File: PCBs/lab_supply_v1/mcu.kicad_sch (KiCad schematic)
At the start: 0 parts

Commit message: Updated PCB, FTDI interface
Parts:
- added C37, C38, C48: 2.2uF, symbol Device:C
- added C39, C40, C41, C42, C45, C46, C47, C49: 100nF, symbol Device:C
- added C43, C44: 1.2pF, symbol Device:C
- added D10, D9: RED, symbol Device:LED
- added FB1: Ferrite_Bead, symbol PCM_Device_AKL:Ferrite_Bead
- added L4: 1.8nH, symbol Device:L
- added R26, R27, R28: 1kR, symbol Device:R_Small
- added R29: 0R, symbol Device:R_Small
- added SW1: EN, symbol Switch:SW_Push
- added U13: ESP32-PICO-D4, Package_DFN_QFN:QFN-48-1EP_7x7mm_P0.5mm_EP5.3x5.3mm, symbol MCU_Espressif:ESP32-PICO-D4
- added U15: FT232RL, Package_SO:SSOP-28_5.3x10.2mm_P0.65mm, symbol Interface_USB:FT232RL
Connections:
- new net: R29.1, U13.26 (VDD_SDIO)
- new net: C38.1, C39.1, C40.1, C41.1, C42.1, FB1.2, U13.1 (VDDA), U13.19 (VDD3P3_RTC), U13.3 (VDDA3P3), U13.37 (VDD3P3_CPU), U13.4 (VDDA3P3), U13.43 (VDDA), U13.46 (VDDA)
- new net: C48.1, R28.2, SW1.2, U13.9 (EN)
- new net: D10.2 (A), R26.1
- new net: D9.2 (A), R27.1
- new net: C43.1, L4.1, U13.2 (LNA_IN)
- new net: C47.1, U15.17 (3V3OUT)
- new net +3.3V: C37.1, C45.1, C46.1, C49.1, FB1.1, R26.2, R27.2, R28.1, R29.2, U15.20 (VCC), U15.4 (VCCIO)
- new net Antenna: C44.1, L4.2
- new net D+: U15.15 (USBD+)
- new net D-: U15.16 (USBD-)
- new net GND: C37.2, C38.2, C39.2, C40.2, C41.2, C42.2, C43.2, C44.2, C45.2, C46.2, C47.2, C48.2, C49.2, SW1.1, U13.49 (GND), U15.18 (GND), U15.21 (GND), U15.25 (AGND), U15.7 (GND)
- new net MCU_CTS: U13.21 (IO15), U15.11 (CTS)
- new net MCU_RTS: U13.20 (IO13), U15.3 (RTS)
- new net MCU_RX: U13.40 (U0RXD/IO3), U15.1 (TXD)
- new net MCU_TX: U13.41 (U0TXD/IO1), U15.5 (RXD)
- new net RX_LED: D10.1 (K), U15.22 (CBUS1)
- new net TX_LED: D9.1 (K), U15.23 (CBUS0)
- no-connect marks 0 -> 13

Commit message: Updated PCB added current sense buffer added ADC/DAC for current/voltage sensing added ACDC converter bypass made optimal supply voltage 36 V @ 5 A
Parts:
- added J6: FAN_OUT, symbol Connector:Screw_Terminal_01x02
- added U16: MCP4922-ESL, PCM_Package_SO_AKL:SOIC-14_3.9x8.7mm_P1.27mm, symbol Analog_DAC:MCP4922-ESL
- added U17: MCP3202, symbol Analog_ADC:MCP3202
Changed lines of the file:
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@@
+	)
+	(symbol
+		(lib_id "Connector:Screw_Terminal_01x02")
+		(at 228.6 133.35 0)
+		(unit 1)
+		(exclude_from_sim no)
+		(in_bom yes)
+		(on_board yes)
+		(dnp no)
+		(fields_autoplaced yes)
+		(property "Reference" "J6"
+			(at 231.14 133.3499 0)
+			(effects
+				(font
+					(size 1.27 1.27)
+				)
+				(justify left)
+			)
+		)
+		(property "Value" "FAN_OUT"
+			(at 231.14 135.8899 0)
+			(effects
+				(font
+					(size 1.27 1.27)
+				)
+				(justify left)
+			)
+		)
+		(property "Footprint" ""
+			(at 228.6 133.35 0)
+			(effects
+				(font
+					(size 1.27 1.27)
+				)
+				(hide yes)
+			)
+		)
+		(property "Datasheet" "~"
+			(at 228.6 133.35 0)
+			(effects
+				(font
+					(size 1.27 1.27)
+				)
+				(hide yes)
+			)
+		)
+		(property "Description" "Generic screw terminal, single row, 01x02, script generated (kicad-library-utils/schlib/autogen/connector/)"
+			(at 228.6 133.35 0)
+			(effects
+				(font
+					(size 1.27 1.27)
+				)
+				(hide yes)
+			)
+		)
+		(pin "2"
+		)
+		(pin "1"
+		)
+		(instances
+			(project "lab_supply_v1"
+				(path "/c381ddef-a21e-4847-9921-7e6cff5e49a3/01eef697-a715-4e9d-9e7c-e0556cbb5130"
+					(reference "J6")
+					(unit 1)
+				)
+			)
+		)
 	)
 	(symbol
@@
 	)
 	(symbol
+		(lib_id "Analog_ADC:MCP3202")
+		(at 66.04 143.51 180)
+		(unit 1)
+		(exclude_from_sim no)
+		(in_bom yes)
+		(on_board yes)
+		(dnp no)
+		(fields_autoplaced yes)
+		(property "Reference" "U17"
+			(at 69.0565 128.27 0)
+			(effects
+				(font
+					(size 1.27 1.27)
+				)
+				(justify right)
+			)
+		)
+		(property "Value" "MCP3202"
+			(at 69.0565 130.81 0)
+			(effects
+				(font
+					(size 1.27 1.27)
+				)
+				(justify right)
+			)
+		)
+		(property "Footprint" ""
+			(at 66.04 140.97 0)
+			(effects
+				(font
+					(size 1.27 1.27)
+				)
+				(hide yes)
+			)
+		)
+		(property "Datasheet" "http://ww1.microchip.com/downloads/en/DeviceDoc/21034D.pdf"
+			(at 66.04 148.59 0)
+			(effects
+				(font
+					(size 1.27 1.27)
+				)
+				(hide yes)
+			)
+		)
+		(property "Description" "A/D Converter, 12-Bit, 2-Channel, SPI Interface, 2.7V-5.5V"
+			(at 66.04 143.51 0)
+			(effects
+				(font
+					(size 1.27 1.27)
+				)
+				(hide yes)
+			)
+		)
+		(pin "2"
+		)
+		(pin "4"
+		)
+		(pin "5"
+		)
+		(pin "6"
+		)
+		(pin "1"
+		)
+		(pin "3"
+		)
+		(pin "7"
+		)
+		(pin "8"
+		)
+		(instances
+			(project "lab_supply_v1"
+				(path "/c381ddef-a21e-4847-9921-7e6cff5e49a3/01eef697-a715-4e9d-9e7c-e0556cbb5130"
+					(reference "U17")
+					(unit 1)
+				)
+			)
+		)
+	)
+	(symbol
 		(lib_id "power:GND")
 		(at 62.23 35.56 0)
@@
 					(unit 1)
 				)
+			)
+		)
+	)
+	(symbol
+		(lib_id "Analog_DAC:MCP4922-ESL")
+		(at 62.23 175.26 0)
+		(unit 1)
+		(exclude_from_sim no)
+		(in_bom yes)
+		(on_board yes)
+		(dnp no)
+		(fields_autoplaced yes)
+		(property "Reference" "U16"
+			(at 86.36 163.8614 0)
+			(effects
+				(font
+					(size 1.27 1.27)
+				)
+			)
+		)
+		(property "Value" "MCP4922-ESL"
+			(at 86.36 166.4014 0)
+			(effects
+				(font
+					(size 1.27 1.27)
+				)
+			)
+		)
+		(property "Footprint" "PCM_Package_SO_AKL:SOIC-14_3.9x8.7mm_P1.27mm"
+			(at 62.23 175.26 0)
+			(effects
+				(font
+					(size 1.27 1.27)
+					(italic yes)
+				)
+				(hide yes)
+			)
+		)
+		(property "Datasheet" "http://ww1.microchip.com/downloads/en/devicedoc/21897a.pdf"
+			(at 62.23 175.26 0)
+			(effects
+				(font
+					(size 1.27 1.27)
+				)
+				(hide yes)
+			)
+		)
+		(property "Description" "Dual 12-bit Digital to Analog Converter, SPI Interface, SOIC-14"
+			(at 62.23 175.26 0)
+			(effects
+				(font
+					(size 1.27 1.27)
+				)
+				(hide yes)
+			)
+		)
+		(pin "3"
+		)
+		(pin "4"
+		)
+		(pin "1"
+		)
+		(pin "10"
+		)
+		(pin "12"
+		)
+		(pin "5"
+		)
+		(pin "2"
+		)
+		(pin "6"
+		)
+		(pin "7"
+		)
+		(pin "8"
+		)
+		(pin "9"
+		)
+		(pin "11"
+		)
+		(pin "13"
+		)
+		(pin "14"
+		)
+		(instances
+			(project "lab_supply_v1"
+				(path "/c381ddef-a21e-4847-9921-7e6cff5e49a3/01eef697-a715-4e9d-9e7c-e0556cbb5130"
+					(reference "U16")
+					(unit 1)
+				)

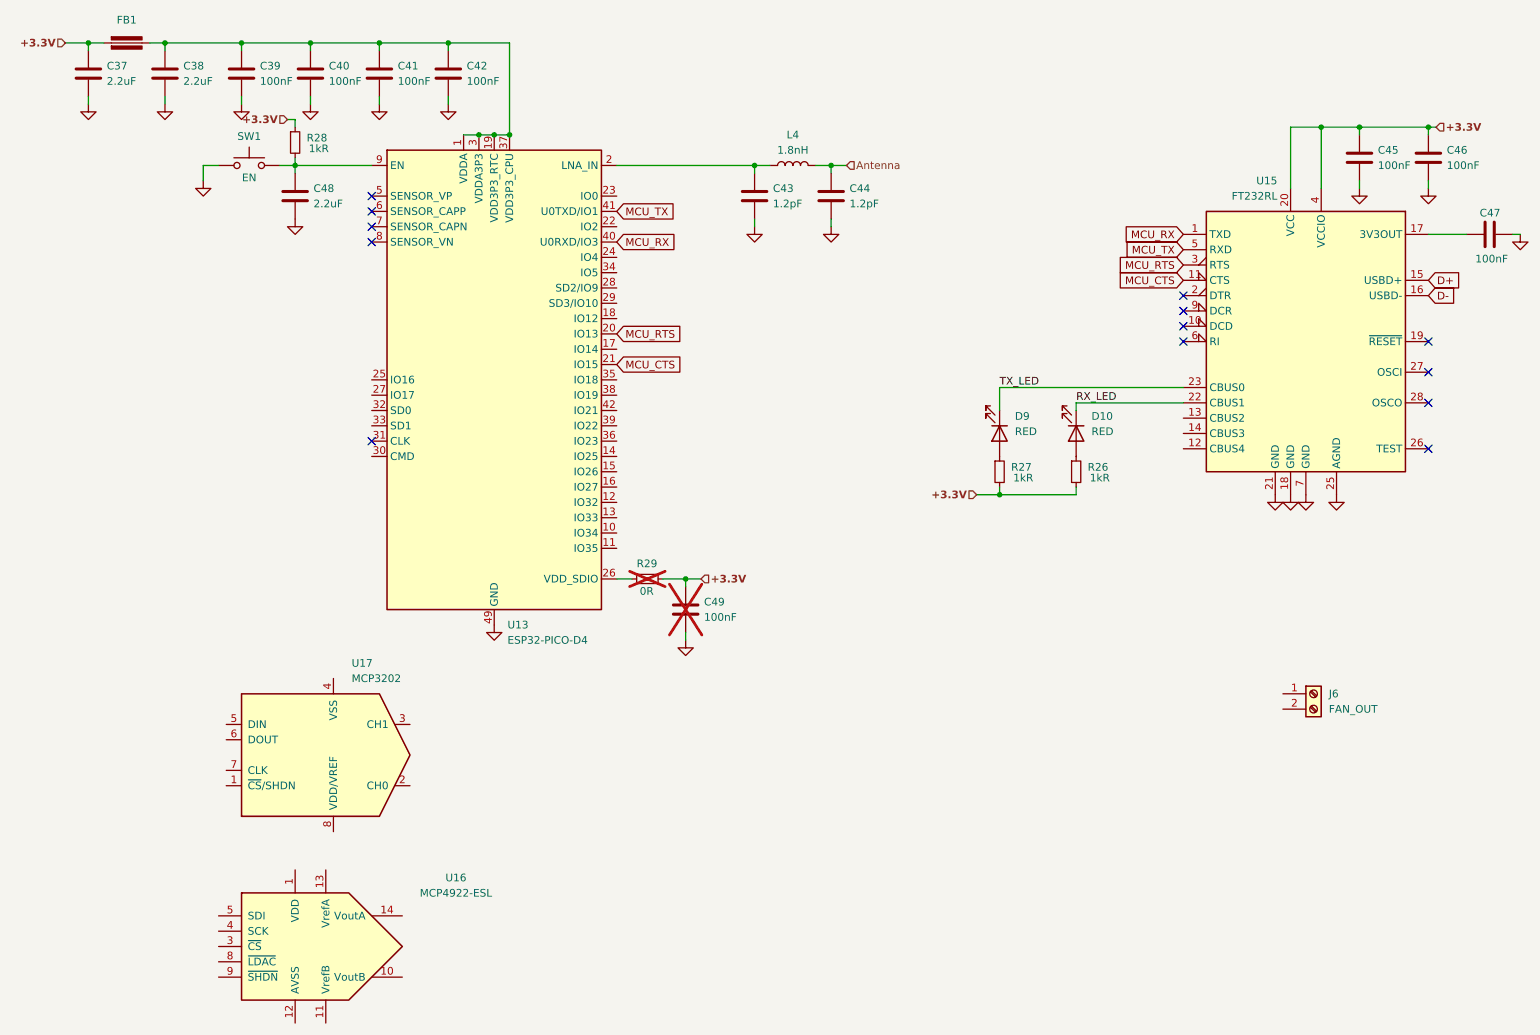
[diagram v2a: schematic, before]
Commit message: Changed MCU to ESP32 WROOM module Added constant current source (3.3 A max, 150 W)
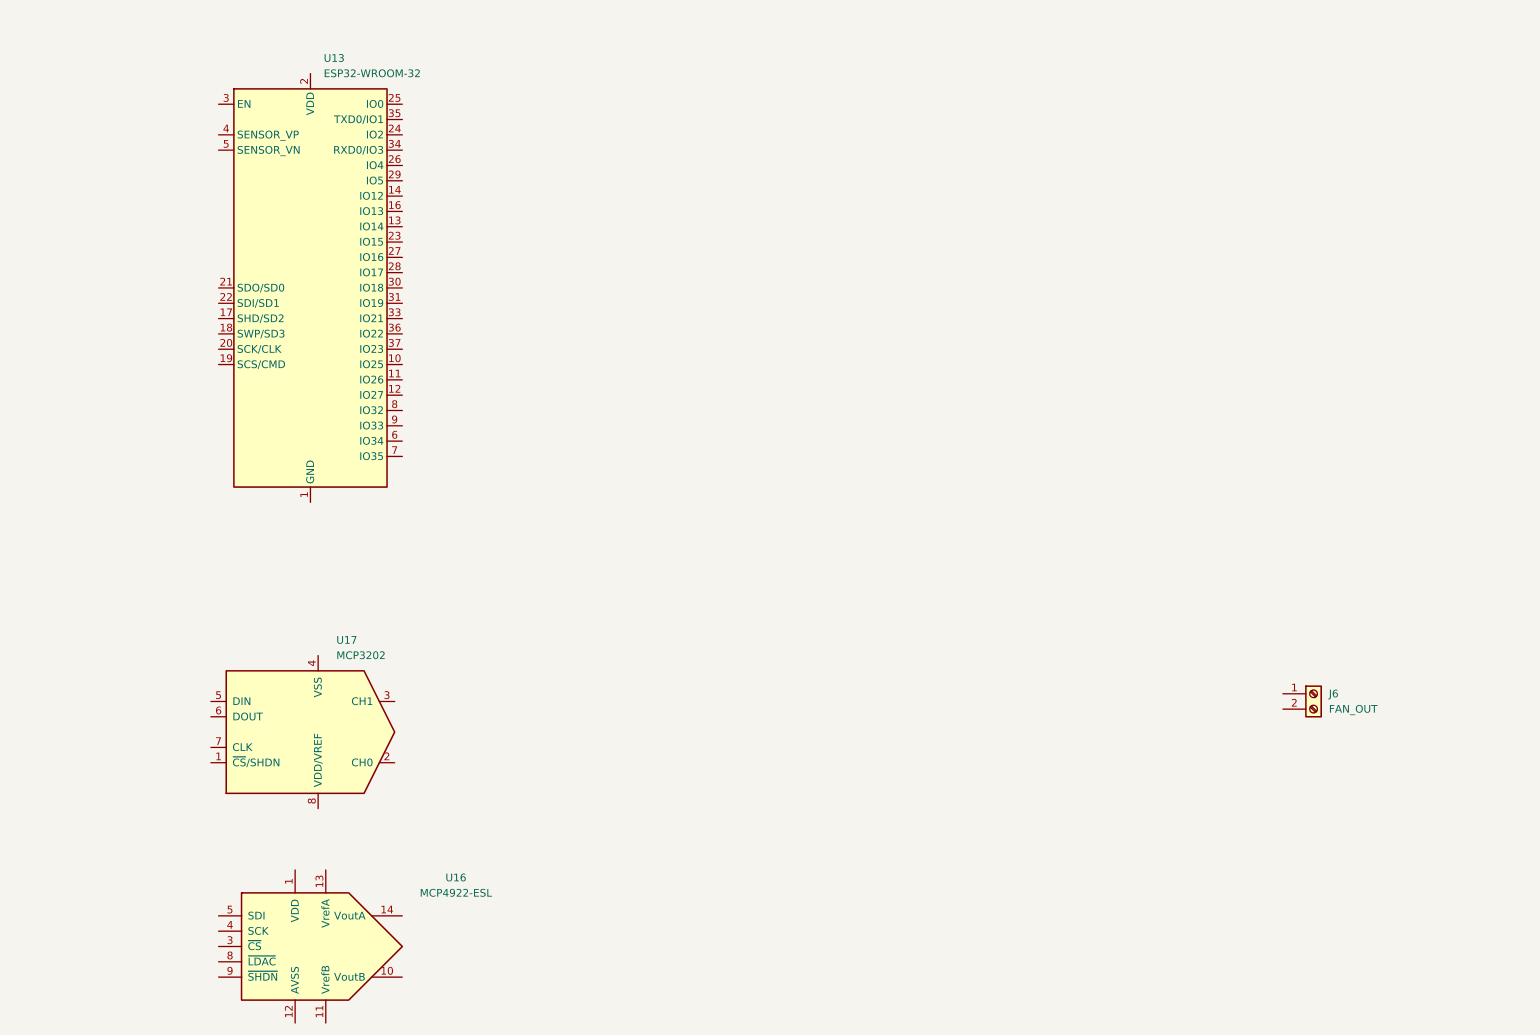
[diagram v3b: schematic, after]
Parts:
- removed C37, C38, C48: 2.2uF, symbol Device:C
- removed C39, C40, C41, C42, C45, C46, C47, C49: 100nF, symbol Device:C
- removed C43, C44: 1.2pF, symbol Device:C
- removed D10, D9: RED, symbol Device:LED
- removed FB1: Ferrite_Bead, symbol PCM_Device_AKL:Ferrite_Bead
- removed L4: 1.8nH, symbol Device:L
- removed R26, R27, R28: 1kR, symbol Device:R_Small
- removed R29: 0R, symbol Device:R_Small
- removed SW1: EN, symbol Switch:SW_Push
- removed U13: ESP32-PICO-D4, Package_DFN_QFN:QFN-48-1EP_7x7mm_P0.5mm_EP5.3x5.3mm, symbol MCU_Espressif:ESP32-PICO-D4
- removed U15: FT232RL, Package_SO:SSOP-28_5.3x10.2mm_P0.65mm, symbol Interface_USB:FT232RL
- added U13: ESP32-WROOM-32, RF_Module:ESP32-WROOM-32, symbol RF_Module:ESP32-WROOM-32
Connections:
- new net: U13.1 (GND), U13.15 (GND), U13.38 (GND), U13.39 (GND)
- no-connect marks 13 -> 0
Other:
- moved on the sheet: U17

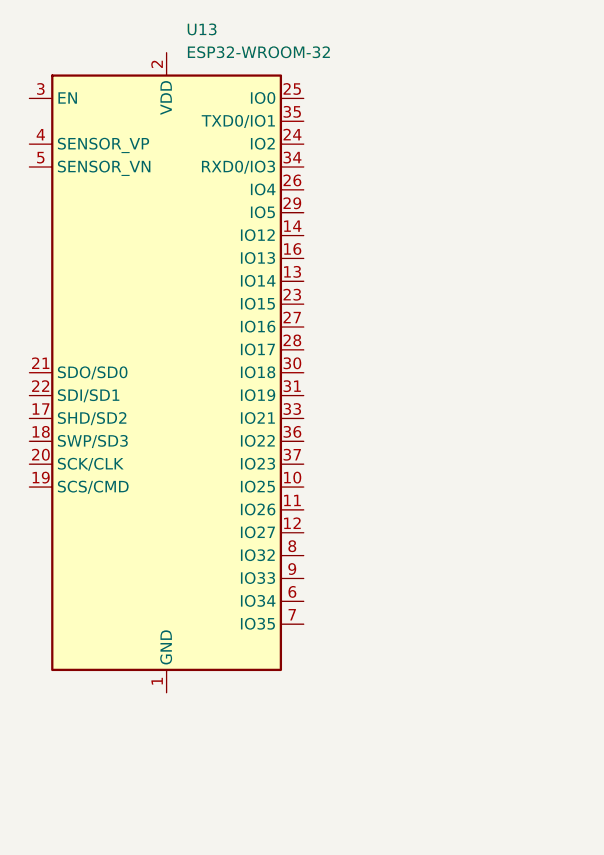
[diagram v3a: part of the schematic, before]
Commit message: added more info to CC sink updated ESP module to fit HiLetgo's ESP32-WROOM
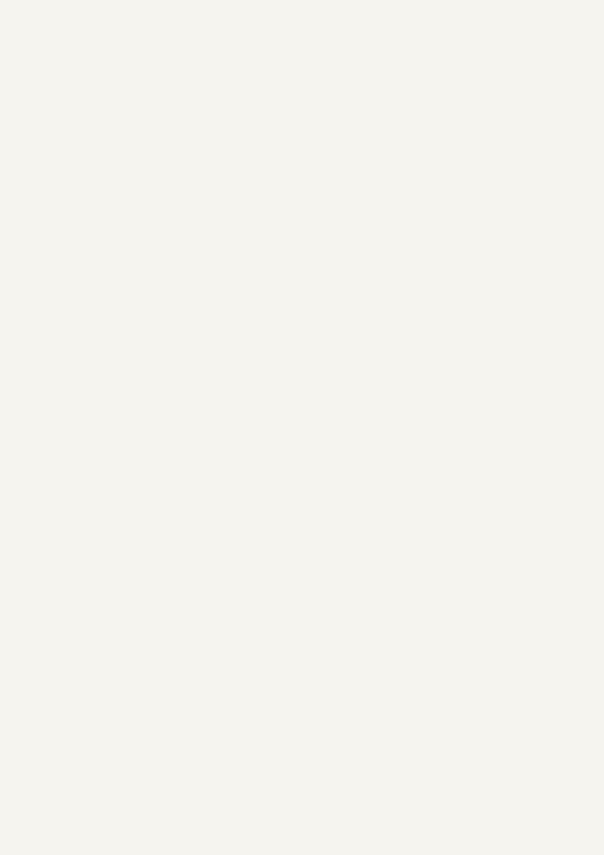
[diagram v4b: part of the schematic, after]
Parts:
- removed U13: ESP32-WROOM-32, RF_Module:ESP32-WROOM-32, symbol RF_Module:ESP32-WROOM-32
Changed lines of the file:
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@@
 	(paper "A4")
-	(symbol
-		(lib_id "RF_Module:ESP32-WROOM-32")
-		(at 62.23 66.04 0)
-		(unit 1)
-		(exclude_from_sim no)
-		(in_bom yes)
-		(on_board yes)
-		(dnp no)
-		(fields_autoplaced yes)
-		(property "Reference" "U13"
-			(at 64.4241 27.94 0)
-			(effects
-				(font
-					(size 1.27 1.27)
-				)
-				(justify left)
-			)
-		)
-		(property "Value" "ESP32-WROOM-32"
-			(at 64.4241 30.48 0)
-			(effects
-				(font
-					(size 1.27 1.27)
-				)
-				(justify left)
-			)
-		)
-		(property "Footprint" "RF_Module:ESP32-WROOM-32"
-			(at 62.23 104.14 0)
-			(effects
-				(font
-					(size 1.27 1.27)
-				)
-				(hide yes)
-			)
-		)
-		(property "Datasheet" "https://www.espressif.com/sites/default/files/documentation/esp32-wroom-32_datasheet_en.pdf"
-			(at 54.61 64.77 0)
-			(effects
-				(font
-					(size 1.27 1.27)
-				)
-				(hide yes)
-			)
-		)
-		(property "Description" "RF Module, ESP32-D0WDQ6 SoC, Wi-Fi 802.11b/g/n, Bluetooth, BLE, 32-bit, 2.7-3.6V, onboard antenna, SMD"
-			(at 62.23 66.04 0)
-			(effects
-				(font
-					(size 1.27 1.27)
-				)
-				(hide yes)
-			)
-		)
-		(pin "11"
-		)
-		(pin "16"
-		)
-		(pin "10"
-		)
-		(pin "37"
-		)
-		(pin "35"
-		)
-		(pin "15"
-		)
-		(pin "32"
-		)
-		(pin "28"
-		)
-		(pin "24"
-		)
-		(pin "12"
-		)
-		(pin "22"
-		)
-		(pin "36"
-		)
-		(pin "18"
-		)
-		(pin "2"
-		)
-		(pin "27"
-		)
-		(pin "20"
-		)
-		(pin "31"
-		)
-		(pin "9"
-		)
-		(pin "7"
-		)
-		(pin "39"
-		)
-		(pin "17"
-		)
-		(pin "29"
-		)
-		(pin "26"
-		)
-		(pin "8"
-		)
-		(pin "19"
-		)
-		(pin "14"
-		)
-		(pin "3"
-		)
-		(pin "30"
-		)
-		(pin "38"
-		)
-		(pin "34"
-		)
-		(pin "13"
-		)
-		(pin "1"
-		)
-		(pin "5"
-		)
-		(pin "6"
-		)
-		(pin "4"
-		)
-		(pin "21"
-		)
-		(pin "25"
-		)
-		(pin "23"
-		)
-		(pin "33"
-		)
-		(instances
-			(project "lab_supply_v1"
-				(path "/c381ddef-a21e-4847-9921-7e6cff5e49a3/01eef697-a715-4e9d-9e7c-e0556cbb5130"
-					(reference "U13")
-					(unit 1)
-				)
-			)
-		)
-	)
 	(symbol
 		(lib_id "Connector:Screw_Terminal_01x02")
